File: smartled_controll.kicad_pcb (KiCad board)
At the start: 2 copper layers, 61.2 x 43.7 mm, 89 parts, among them J1 Conn_01x04, SW1 SW_Push, U1 OC5028B, U2 MAX485E, U3 PY32F003F1xUx, U4 OC5864, U5 need chooice, U6 OC5028B, U7 need chooice, U8 OC5028B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

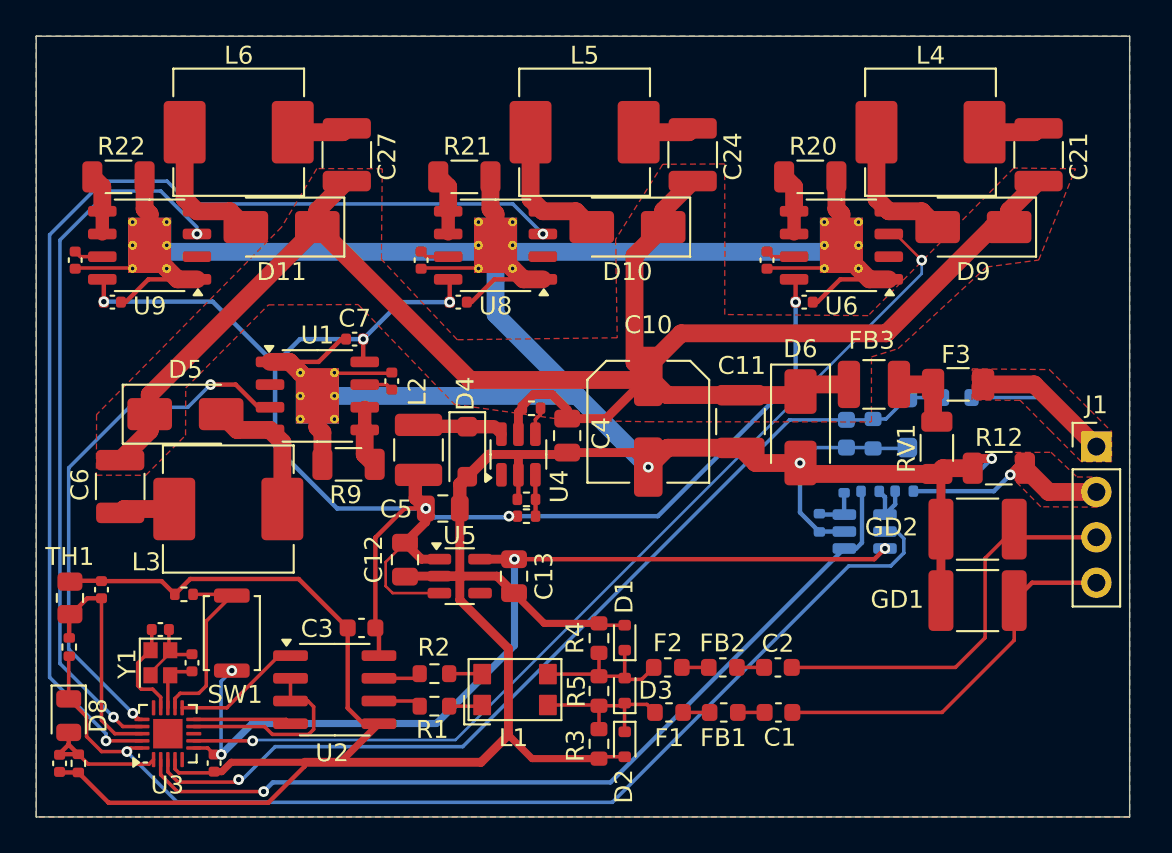
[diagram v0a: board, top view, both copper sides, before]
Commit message: 添加LED驱动输入滤波电容(1210封装)
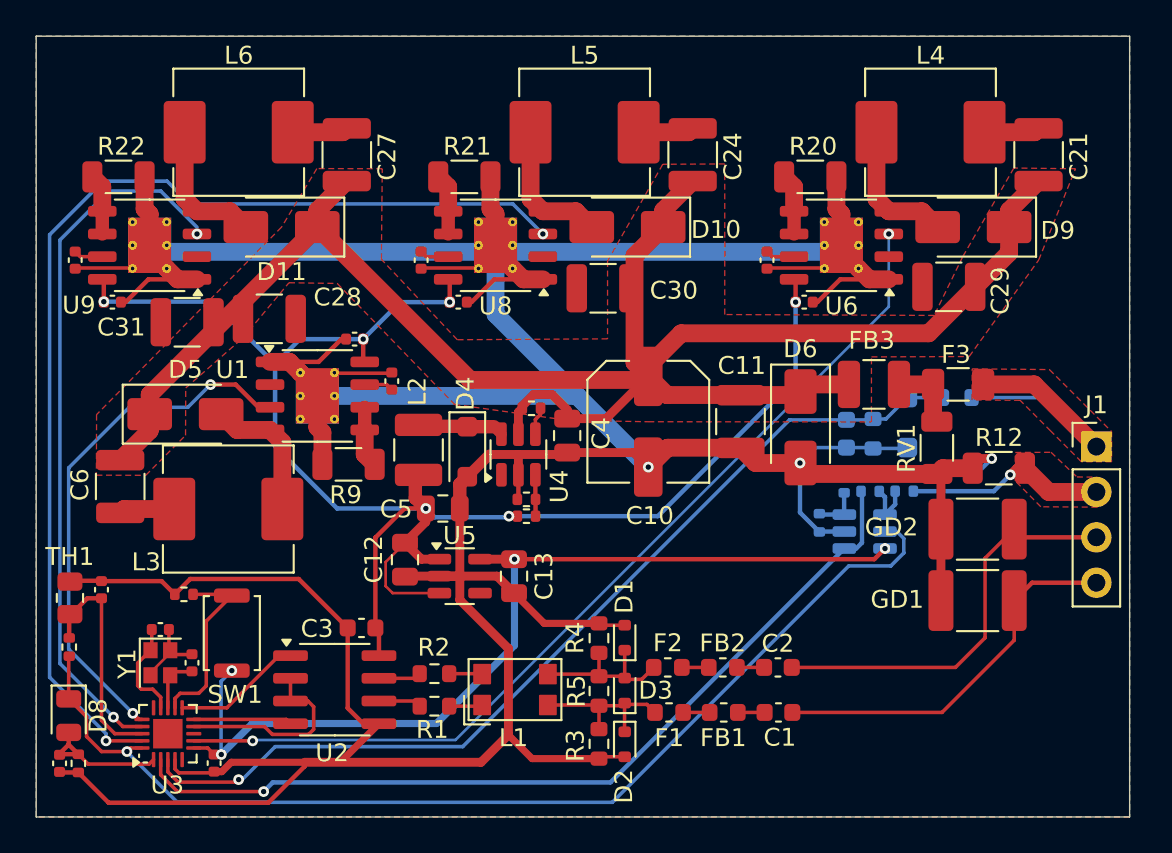
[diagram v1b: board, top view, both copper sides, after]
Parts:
- added C28: C, Capacitor_SMD:C_1210_3225Metric, F.Cu at (145.4, 67.8)
- added C29: C, Capacitor_SMD:C_1210_3225Metric, F.Cu at (183.5, 66.0)
- added C30: C, Capacitor_SMD:C_1210_3225Metric, F.Cu at (164.1, 66.1)
- added C31: C, Capacitor_SMD:C_1210_3225Metric, F.Cu at (140.8, 68.0)
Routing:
- net /PWM2: track 54.8 -> 53.0 mm
- net VINP: track 105.6 -> 106.4 mm

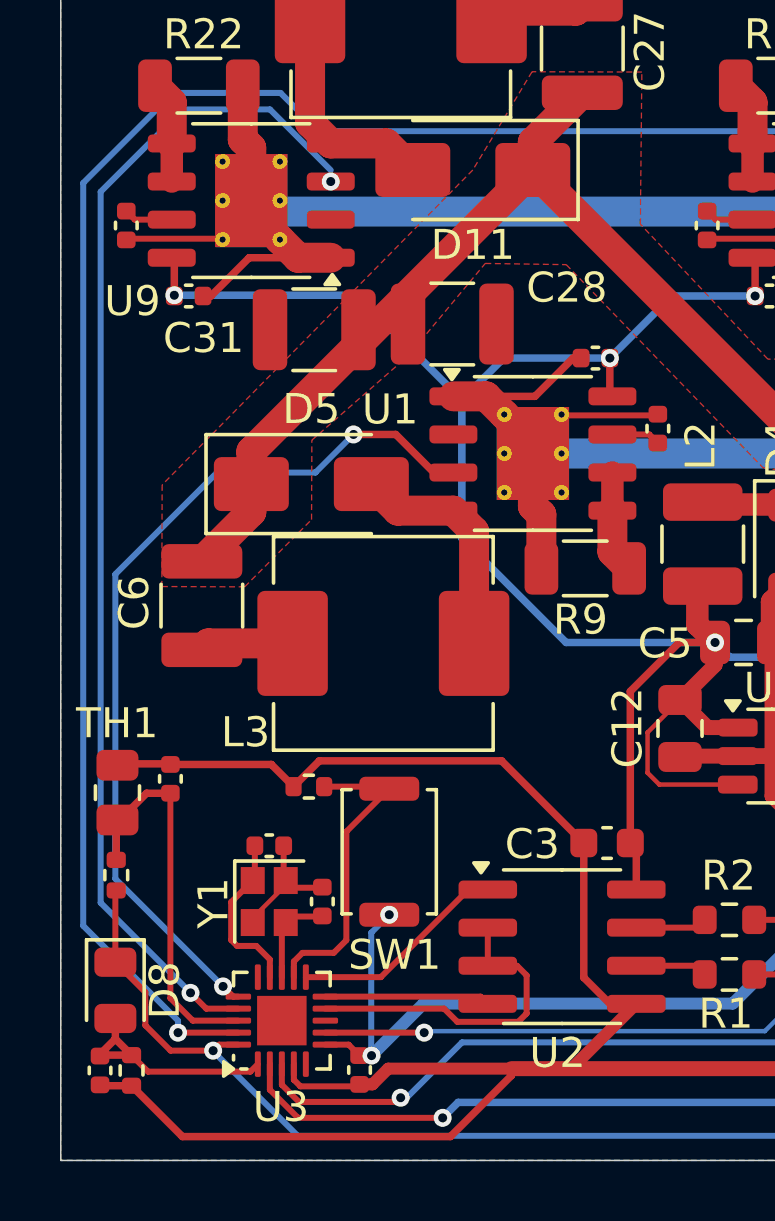
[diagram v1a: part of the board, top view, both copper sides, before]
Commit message: 添加I2C接口
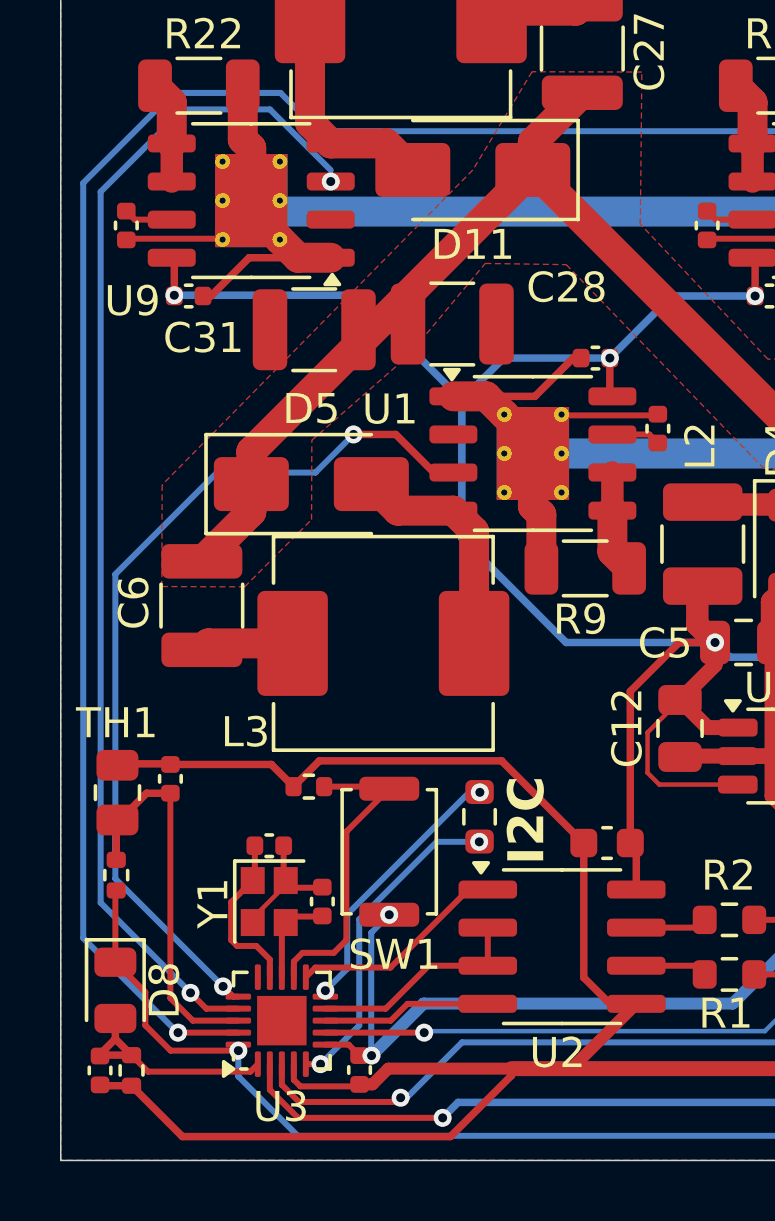
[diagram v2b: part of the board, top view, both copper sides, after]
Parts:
- added J2: Conn_01x02, Resistor_SMD:R_0603_1608Metric, F.Cu at (146.4, 84.2)
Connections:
- U3 pad 10: /MAX485_DI -> /I2C_SCL
- U3 pad 5: unconnected-(U3-PA12-Pad5) -> /I2C_SDA
- U3 pad 8: unconnected-(U3-PA14_SWC-Pad8) -> /MAX485_DI
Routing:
- net /I2C_SDA: track 0.00 -> 10.9 mm, vias 0 -> 2
- net /I2C_SCL: track 0.00 -> 9.15 mm, vias 0 -> 2
- net /MAX485_TR: track 11.0 -> 7.28 mm
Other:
- board text added: "I2C"

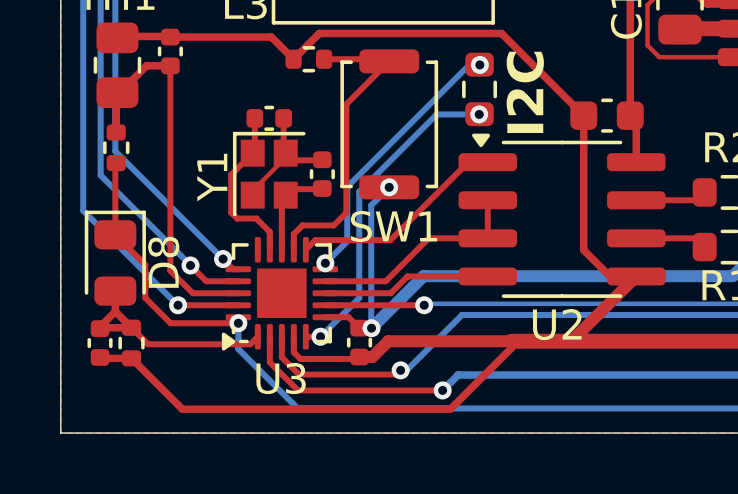
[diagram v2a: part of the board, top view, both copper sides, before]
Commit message: 按照数据手册将PY32中心焊盘接GND
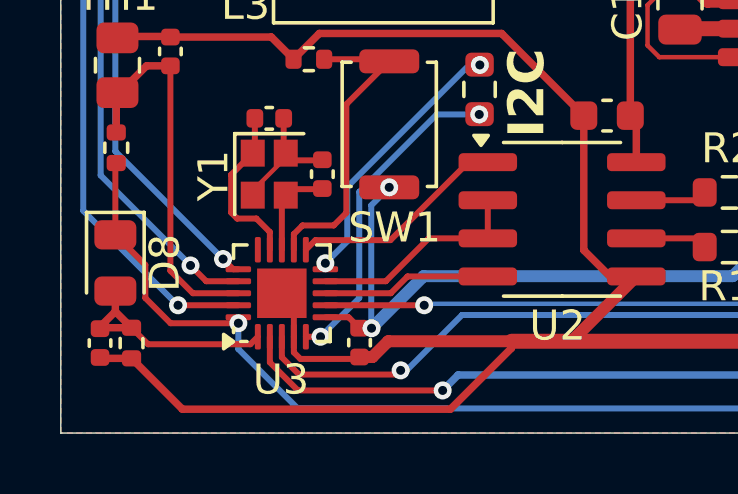
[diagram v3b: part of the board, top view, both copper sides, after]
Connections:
- U3 pad 21: (no net) -> GND
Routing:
- net GND: track 305.5 -> 307.1 mm
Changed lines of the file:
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@@
 			(property pad_prop_heatsink)
 			(layers "F.Cu" "F.Mask")
+			(net 5 "GND")
+			(pinfunction "EP")
+			(pintype "passive")
 			(zone_connect 2)
 		)
@@
 	)
 	(segment
+		(start 140.17 92.49)
+		(end 140.17 91.44)
+		(width 0.2)
+		(layer "F.Cu")
+		(net 5)
+	)
+	(segment
 		(start 149.48325 68.955)
 		(end 148.20825 70.23)
@@
 		(width 0.2)
 		(layer "F.Cu")
+		(net 5)
+	)
+	(segment
+		(start 140.17 91.44)
+		(end 139.77 91.04)
+		(width 0.2)
+		(layer "F.Cu")

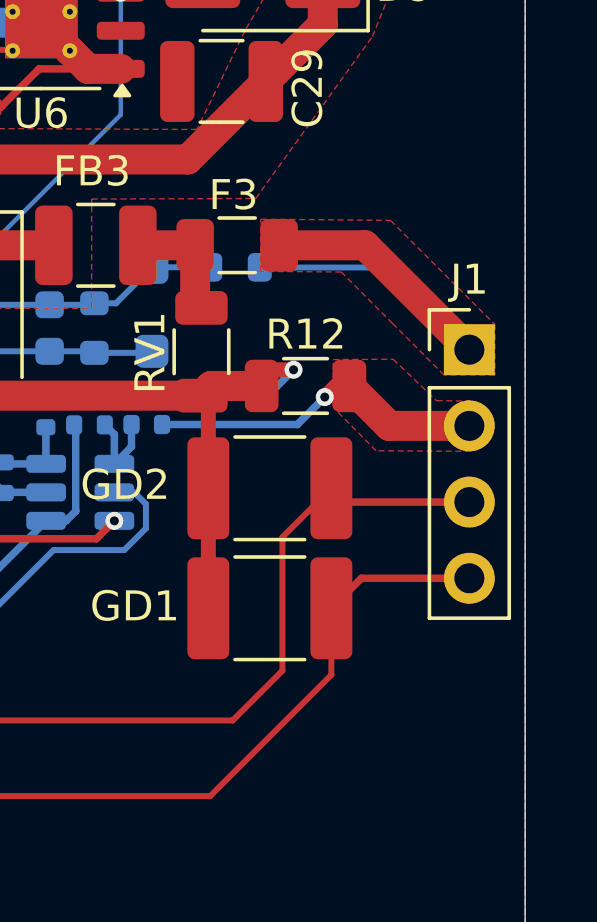
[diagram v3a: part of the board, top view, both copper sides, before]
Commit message: PCB上添加接口定义和版权声明文本
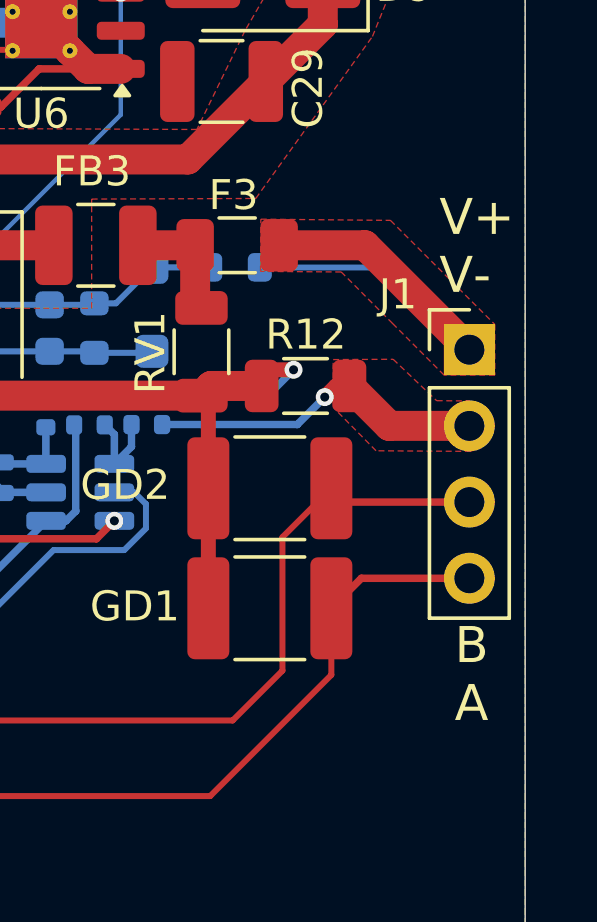
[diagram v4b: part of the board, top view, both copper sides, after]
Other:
- board text added: "B A"
- board text added: "Copyright (C) 2025 Xu Ruijun License under CERN-OHL-S v2 https://github.com/XuHg-zjcn/smartled_controll"
- board text added: "V+ V-"
- board text added: "V+ V- B A"
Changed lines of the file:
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@@
 		(tags "Through hole pin header THT 1x04 2.54mm single row")
 		(property "Reference" "J1"
-			(at 0 -2.33 0)
+			(at -2.38 -1.84 0)
 			(layer "F.SilkS")
 			(effects
@@
 		(layer "Edge.Cuts")
 	)
+	(gr_text "V+\nV-\nB\nA"
+		(at 190.46 78.86 0)
+		(layer "B.SilkS")
+		(effects
+			(font
+				(size 1.2 1.2)
+				(thickness 0.15)
+			)
+			(justify left mirror)
+		)
+	)
+	(gr_text "Copyright (C) 2025  Xu Ruijun\nLicense under CERN-OHL-S v2\nhttps://github.com/XuHg-zjcn/smartled_controll"
+		(at 183.69 90.05 0)
+		(layer "B.SilkS")
+		(effects
+			(font
+				(size 1 1)
+				(thickness 0.1)
+			)
+			(justify left bottom mirror)
+		)
+	)
+	(gr_text "V+\nV-"
+		(at 190.74 73.19 0)
+		(layer "F.SilkS")
+		(effects
+			(font
+				(size 1.2 1.2)
+				(thickness 0.15)
+			)
+			(justify left bottom)
+		)
+	)
+	(gr_text "B\nA"
+		(at 191.25 87.46 0)
+		(layer "F.SilkS")
+		(effects
+			(font
+				(size 1.2 1.2)
+				(thickness 0.15)
+			)
+			(justify left bottom)
+		)
+	)
 	(gr_text "I2C"

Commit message: 按OC5028B数据手册将第二脚NC改成不连接
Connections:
- U1 pad 2: GND -> unconnected-(U1-NC-Pad2)
- U6 pad 2: GND -> unconnected-(U6-NC-Pad2)
- U8 pad 2: GND -> unconnected-(U8-NC-Pad2)
- U9 pad 2: GND -> unconnected-(U9-NC-Pad2)
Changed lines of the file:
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@@
 	(net 60 "Net-(R21-Pad1)")
 	(net 61 "Net-(R22-Pad1)")
+	(net 62 "unconnected-(U1-NC-Pad2)")
+	(net 63 "unconnected-(U6-NC-Pad2)")
+	(net 64 "unconnected-(U8-NC-Pad2)")
+	(net 65 "unconnected-(U9-NC-Pad2)")
 	(footprint "Fuse:Fuse_0603_1608Metric"
 		(layer "F.Cu")
@@
 			(layers "F.Cu" "F.Paste" "F.Mask")
 			(roundrect_rratio 0.25)
-			(net 5 "GND")
+			(net 64 "unconnected-(U8-NC-Pad2)")
 			(pinfunction "NC")
 			(pintype "passive")
@@
 			(layers "F.Cu" "F.Paste" "F.Mask")
 			(roundrect_rratio 0.25)
-			(net 5 "GND")
+			(net 65 "unconnected-(U9-NC-Pad2)")
 			(pinfunction "NC")
 			(pintype "passive")
@@
 			(layers "F.Cu" "F.Paste" "F.Mask")
 			(roundrect_rratio 0.25)
-			(net 5 "GND")
+			(net 62 "unconnected-(U1-NC-Pad2)")
 			(pinfunction "NC")
 			(pintype "passive")
@@
 			(layers "F.Cu" "F.Paste" "F.Mask")
 			(roundrect_rratio 0.25)
-			(net 5 "GND")
+			(net 63 "unconnected-(U6-NC-Pad2)")
 			(pinfunction "NC")
 			(pintype "passive")

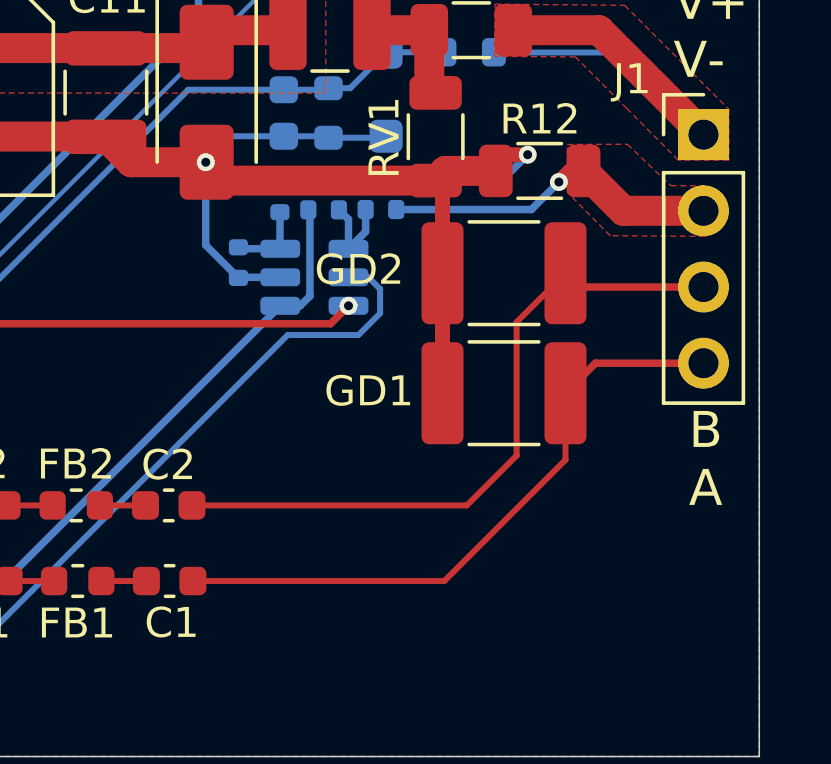
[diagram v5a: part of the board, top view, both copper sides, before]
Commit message: 在RS485的两条差分线间再添加一个气体放电管，都改为1206封装
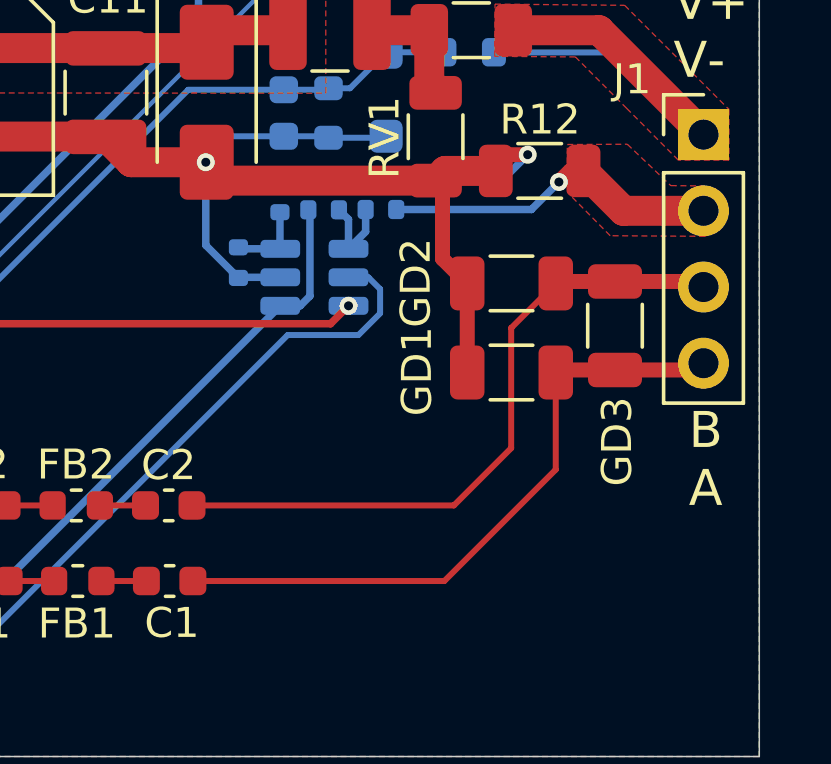
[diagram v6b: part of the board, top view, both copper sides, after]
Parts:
- added GD3: GDT_2Pin, Capacitor_SMD:C_1206_3216Metric, F.Cu at (188.8, 81.3)
- GD1, GD2: footprint Capacitor_SMD:C_1812_4532Metric -> Capacitor_SMD:C_1206_3216Metric
- moved GD1 0.73 mm to (185.3, 82.9)
- moved GD2 0.42 mm to (185.3, 79.9)
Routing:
- net /485+: track 21.3 -> 21.9 mm

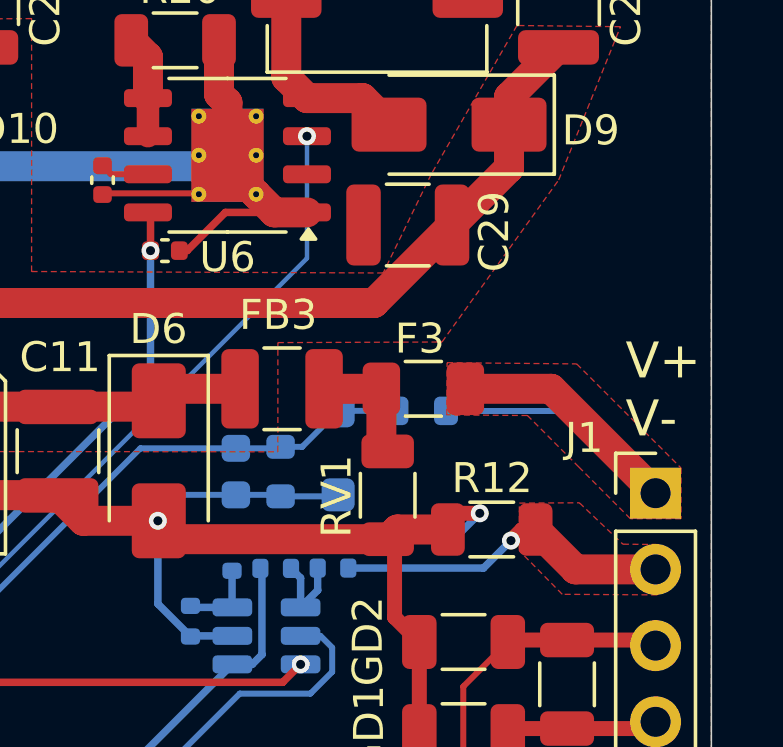
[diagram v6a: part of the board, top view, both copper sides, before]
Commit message: 保险丝改成2410(6125)封装
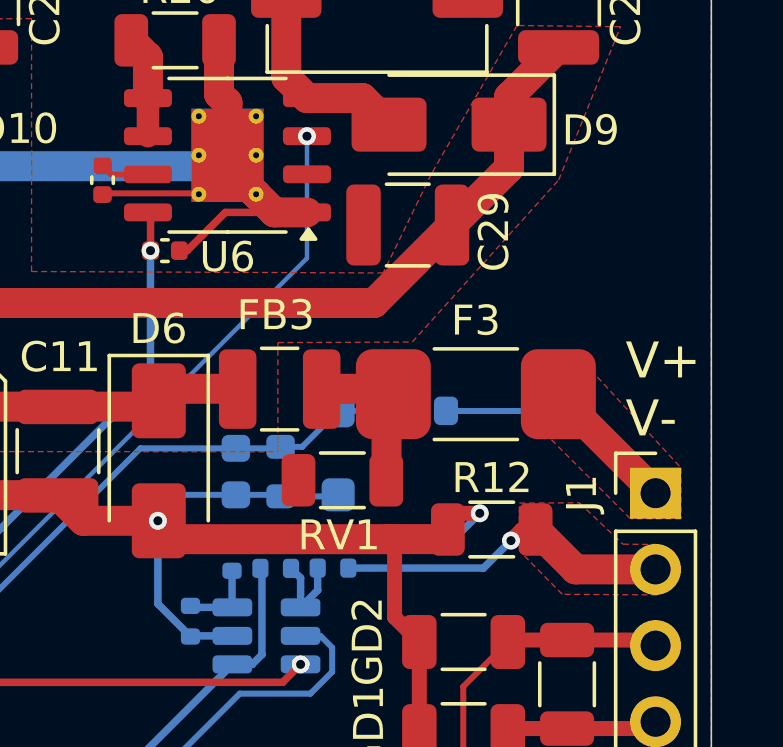
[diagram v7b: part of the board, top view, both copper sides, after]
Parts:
- F3: footprint Fuse:Fuse_1206_3216Metric -> project_footprints:Fuse_2410_6125Metric
- moved F3 1.76 mm to (185.8, 71.7)
- moved RV1 1.59 mm to (181.3, 74.5), turned to 180 degrees
- moved FB3 0.08 mm to (179.2, 71.5)
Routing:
- net /VIN+: track 15.9 -> 12.8 mm
- net Net-(F3-Pad2): track 4.08 -> 5.12 mm
